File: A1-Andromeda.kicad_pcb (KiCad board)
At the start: 2 copper layers, 96 x 40 mm, 34 parts, among them J1 Conn_01x02, J2 Conn_01x02, J3 Conn_01x02, J4 Conn_01x03_Socket, J5 Conn_01x10_Pin, J6 Conn_01x10_Pin, J8 Conn_01x10_Pin, SW1 SW_SPST, SW2 SW_DIP_x02, U1 LM2940IMPX-5.0/NOPB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

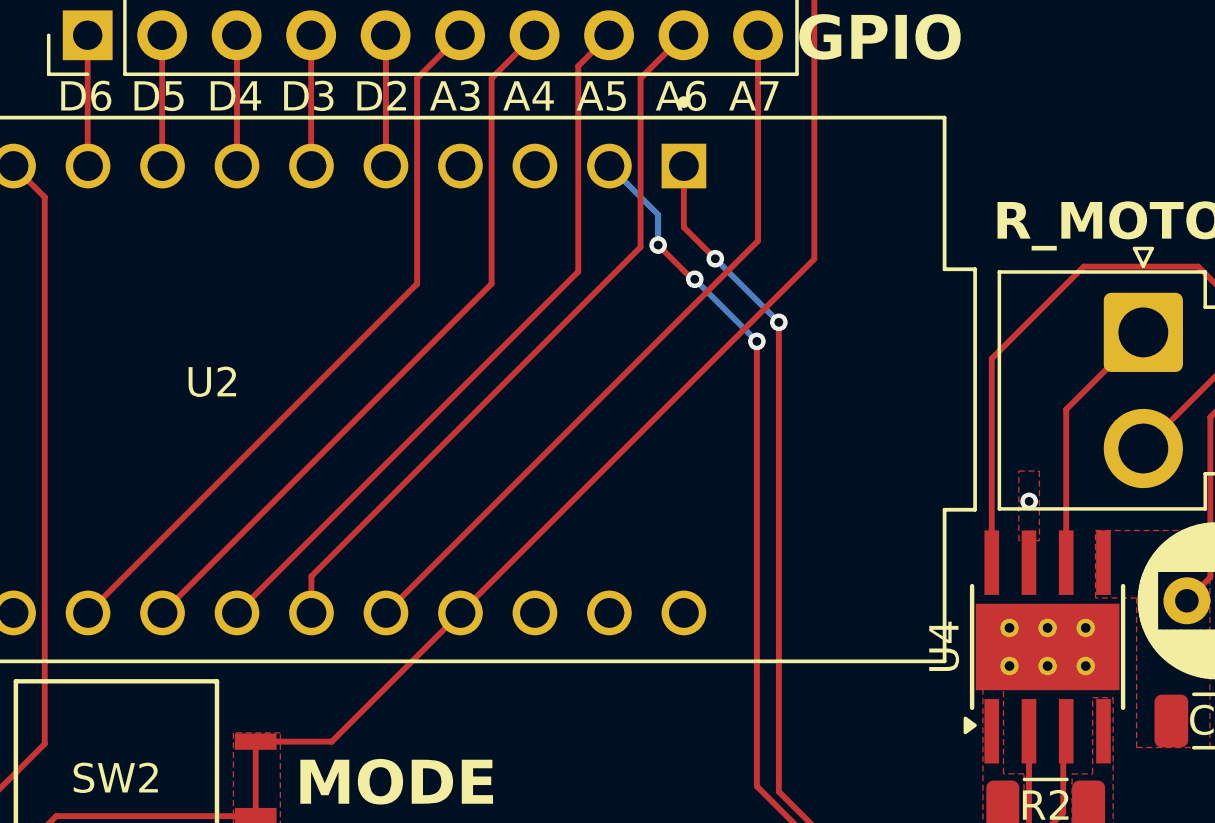
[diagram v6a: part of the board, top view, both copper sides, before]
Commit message: fix VIN
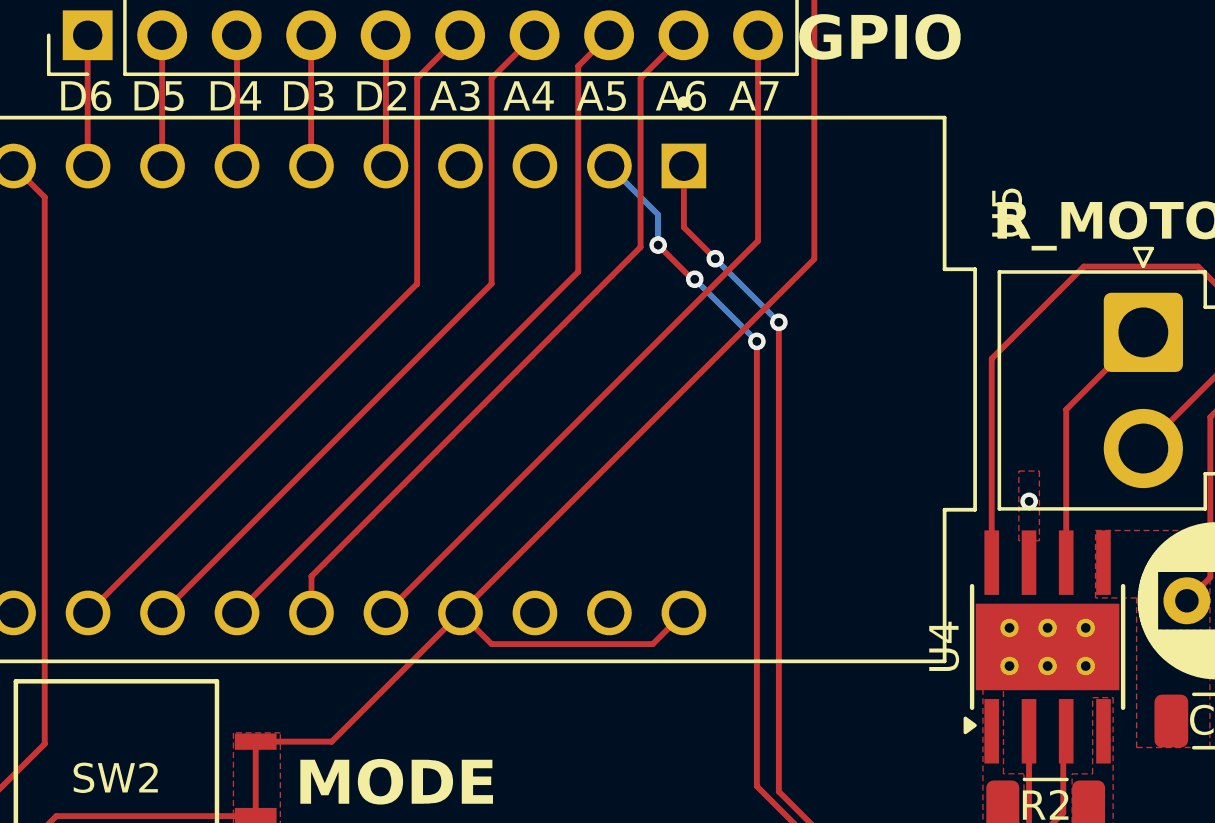
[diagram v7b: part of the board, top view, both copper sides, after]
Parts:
- removed U2: NUCLEO-F042K6, footprints:MODULE_NUCLEO-F042K6
- added U5: NUCLEO-F042K6, footprints:MODULE_NUCLEO-F042K6, F.Cu at (146.1, 89.5)
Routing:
- net +5V: track 148.3 -> 156.8 mm

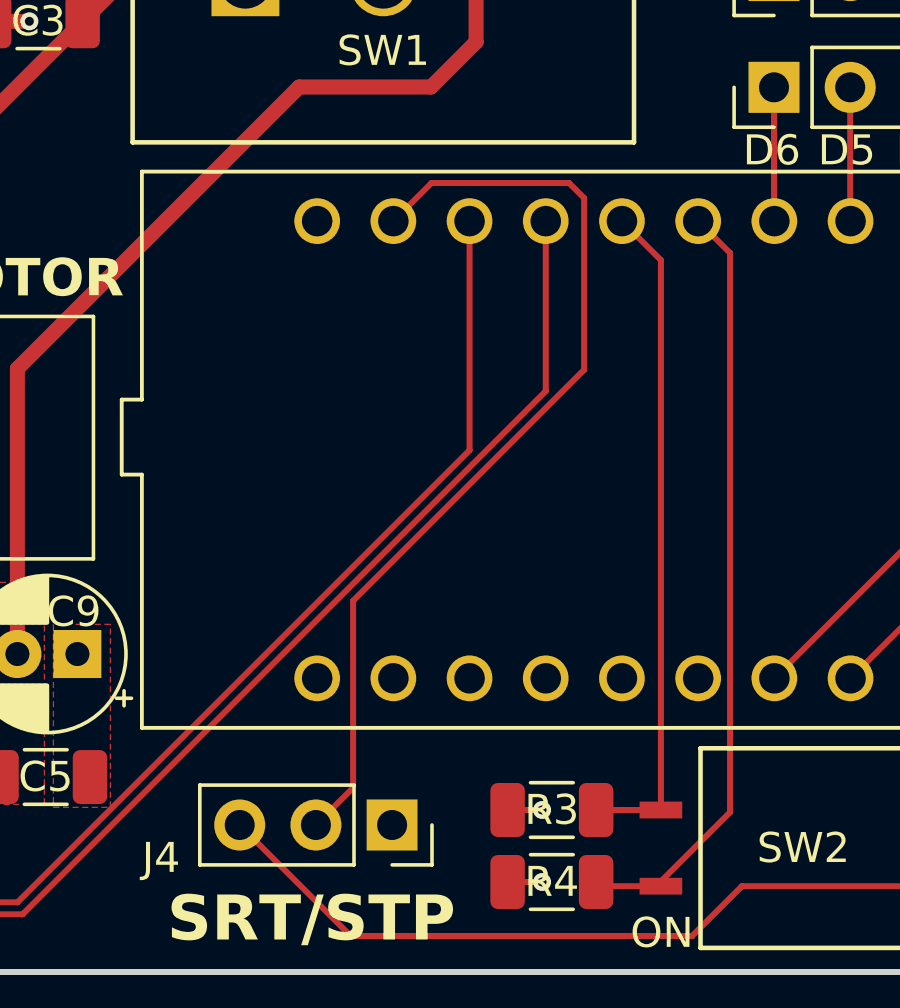
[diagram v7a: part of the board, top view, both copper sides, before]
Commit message: fix start/stop module pins
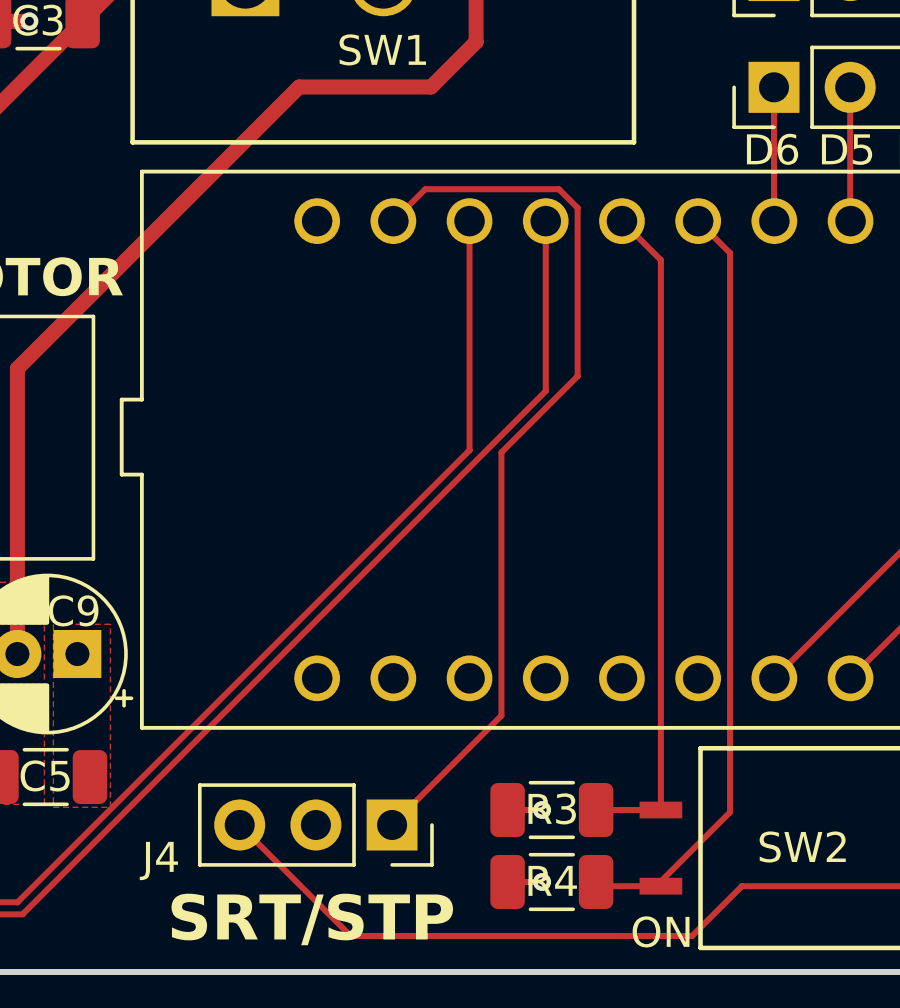
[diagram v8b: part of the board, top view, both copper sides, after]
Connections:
- J4 pad 1: GND -> /SRT_STP_MODULE
- J4 pad 2: /SRT_STP_MODULE -> GND
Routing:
- net /SRT_STP_MODULE: track 31.7 -> 30.0 mm
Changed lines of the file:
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@@
 			(layers "*.Cu" "*.Mask")
 			(remove_unused_layers no)
-			(net 24 "GND")
+			(net 2 "/SRT_STP_MODULE")
 			(pinfunction "Pin_1")
 			(pintype "passive")
@@
 			(layers "*.Cu" "*.Mask")
 			(remove_unused_layers no)
-			(net 2 "/SRT_STP_MODULE")
+			(net 24 "GND")
 			(pinfunction "Pin_2")
 			(pintype "passive")
@@
 	)
 	(segment
-		(start 135.7 81.1)
-		(end 135.7 86.826304)
+		(start 132.945 98.355)
+		(end 132.945 89.581304)
 		(width 0.2)
 		(layer "F.Cu")
@@
 	)
 	(segment
-		(start 128 100.76)
-		(end 126.76 102)
+		(start 130.405 80.808)
+		(end 129.342 81.871)
 		(width 0.2)
 		(layer "F.Cu")
@@
 	)
 	(segment
-		(start 130.613 80.6)
-		(end 135.2 80.6)
+		(start 135.485 81.43069)
+		(end 134.86231 80.808)
 		(width 0.2)
 		(layer "F.Cu")
@@
 	)
 	(segment
-		(start 128 94.526304)
-		(end 128 100.76)
+		(start 129.3 102)
+		(end 132.945 98.355)
 		(width 0.2)
 		(layer "F.Cu")
@@
 	)
 	(segment
-		(start 135.7 86.826304)
-		(end 128 94.526304)
+		(start 134.86231 80.808)
+		(end 130.405 80.808)
 		(width 0.2)
 		(layer "F.Cu")
@@
 	)
 	(segment
-		(start 135.2 80.6)
-		(end 135.7 81.1)
+		(start 132.945 89.581304)
+		(end 135.485 87.041304)
 		(width 0.2)
 		(layer "F.Cu")
@@
 	)
 	(segment
-		(start 129.342 81.871)
-		(end 130.613 80.6)
+		(start 135.485 87.041304)
+		(end 135.485 81.43069)
 		(width 0.2)
 		(layer "F.Cu")
